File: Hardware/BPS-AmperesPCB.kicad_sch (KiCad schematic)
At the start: 54 parts, among them IC1 INA241A5IDR, IC5 AMC1350DWVR, J1 Discharge V_In, J2 PeripheralCAN, J3 Charge V_In, J4 PeripheralCAN, J5 Shunt Conn, U1 INA145UA/2K5, U2 AMC1300BDWV, U6 TLV6001DCK

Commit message: comments
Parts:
- removed LOGO1: aniMegamind, UTSVT_Logos:Hallock_Image_Small, symbol utsvt-misc:Logo_Placeholder
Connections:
- net OUTN: no longer names the net of R5.2
- net OUTP: no longer names the net of R7.2
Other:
- note added: "Gain: 2.5 V/V (??) Vout = 2.5(VoutP - VoutN) + Vref Cutoff freq: figure out Output voltage range: 0 - 3.3V"
- note added: "TODO: use full 5V input ?? - buck and ldo to 5V"
- note added: "integrate jumper later"
- note removed: "Gain: 2.5 V/V (??) Vout = 2.5(VoutP - VoutN) + Vref Cutoff freq: figure out"
- note removed: "TODO: use full 5V input - buck and ldo to 5V"
- moved on the sheet: H1, H2
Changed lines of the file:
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@@
 	(text "Gain: 0.4 V/V\nInput Voltage Range: 0 - 3.3 V\nOutput Voltage Range: 0 - 1.32 V"
 		(exclude_from_sim no)
-		(at 139.7 130.81 0)
+		(at 139.7 134.62 0)
 		(effects
 			(font
@@
 	(text "Difference amp\nVout = (R2/R1) * (Vp - Vn)"
 		(exclude_from_sim no)
-		(at 220.98 145.034 0)
+		(at 292.354 138.43 0)
 		(effects
 			(font
@@
 		)
 	)
-	(text "Gain: 2.5 V/V (??)\nVout = 2.5(VoutP - VoutN) + Vref\nCutoff freq: figure out "
+	(text "Gain: 2.5 V/V (??)\nVout = 2.5(VoutP - VoutN) + Vref\nCutoff freq: figure out \nOutput voltage range: 0 - 3.3V"
 		(exclude_from_sim no)
-		(at 220.98 135.89 0)
+		(at 221.234 134.874 0)
 		(effects
 			(font
@@
 		)
 	)
-	(text "TODO: use full 5V input\n- buck and ldo to 5V"
+	(text "TODO: use full 5V input ??\n- buck and ldo to 5V"
 		(exclude_from_sim no)
 		(at 151.13 150.876 0)
@@
 		)
 	)
+	(text "integrate jumper later"
+		(exclude_from_sim no)
+		(at 231.14 53.34 0)
+		(effects
+			(font
+				(size 1.27 1.27)
+			)
+		)
+	)
 	(text "(TBD) Shunt Resistor Between 1 and 2\n- old value was 250 uOhm\n"
 		(exclude_from_sim no)
@@
 		)
 	)
-	(label "OUTN"
-		(at 320.04 99.06 0)
-		(effects
-			(font
-				(size 1.27 1.27)
-			)
-			(justify left bottom)
-		)
-	)
 	(label "CAN_HIGH"
 		(at 170.18 55.88 180)
@@
 		)
 	)
-	(label "OUTP"
-		(at 320.04 106.68 0)
-		(effects
-			(font
-				(size 1.27 1.27)
-			)
-			(justify left bottom)
-		)
-	)
 	(label "V-"
 		(at 222.25 59.69 0)
@@
 	(symbol
 		(lib_id "Mechanical:MountingHole")
-		(at 252.73 48.26 0)
+		(at 252.73 39.37 0)
 		(unit 1)
 		(exclude_from_sim no)
@@
 		(fields_autoplaced yes)
 		(property "Reference" "H2"
-			(at 255.27 46.9899 0)
+			(at 255.27 38.0999 0)
 			(effects
 				(font
@@
 		)
 		(property "Value" "ShuntHole2"
-			(at 255.27 49.5299 0)
+			(at 255.27 40.6399 0)
 			(effects
 				(font
@@
 		)
 		(property "Footprint" ""
-			(at 252.73 48.26 0)
+			(at 252.73 39.37 0)
 			(effects
 				(font
@@
 		)
 		(property "Datasheet" "~"
-			(at 252.73 48.26 0)
+			(at 252.73 39.37 0)
 			(effects
 				(font
@@
 		)
 		(property "Description" "Mounting Hole without connection"
-			(at 252.73 48.26 0)
+			(at 252.73 39.37 0)
 			(effects
 				(font
@@
 	(symbol
 		(lib_id "Mechanical:MountingHole")
-		(at 252.73 40.64 0)
+		(at 252.73 31.75 0)
 		(unit 1)
 		(exclude_from_sim no)
@@
 		(dnp no)
 		(property "Reference" "H1"
-			(at 255.27 39.3699 0)
+			(at 255.27 30.4799 0)
 			(effects
 				(font
@@
 		)
 		(property "Value" "ShuntHole1"
-			(at 255.27 41.9099 0)
+			(at 255.27 33.0199 0)
 			(effects
 				(font
@@
 		)
 		(property "Footprint" ""
-			(at 252.73 40.64 0)
+			(at 252.73 31.75 0)
 			(effects
 				(font
@@
 		)
 		(property "Datasheet" "~"
-			(at 252.73 40.64 0)
+			(at 252.73 31.75 0)
 			(effects
 				(font
@@
 		)
 		(property "Description" "Mounting Hole without connection"
-			(at 252.73 40.64 0)
+			(at 252.73 31.75 0)
 			(effects
 				(font
@@
 	)
 	(symbol
-		(lib_id "utsvt-misc:Logo_Placeholder")
-		(at 252.73 21.59 0)
-		(unit 1)
-		(exclude_from_sim no)
-		(in_bom yes)
-		(on_board yes)
-		(dnp no)
-		(fields_autoplaced yes)
-		(property "Reference" "LOGO1"
-			(at 252.73 17.78 0)
-			(effects
-				(font
-					(size 1.27 1.27)
-				)
-				(hide yes)
-			)
-		)
-		(property "Value" "aniMegamind"
-			(at 256.54 21.5899 0)
-			(effects
-				(font
-					(size 1.27 1.27)
-				)
-				(justify left)
-			)
-		)
-		(property "Footprint" "UTSVT_Logos:Hallock_Image_Small"
-			(at 252.73 19.685 0)
-			(effects
-				(font
-					(size 1.27 1.27)
-				)
-				(hide yes)
-			)
-		)
-		(property "Datasheet" ""
-			(at 252.73 19.685 0)
-			(effects
-				(font
-					(size 1.27 1.27)
-				)
-				(hide yes)
-			)
-		)
-		(property "Description" "Graph footprint placeholder"
-			(at 252.73 21.59 0)
-			(effects
-				(font
-					(size 1.27 1.27)
-				)
-				(hide yes)
-			)
-		)
-		(property "PN" ""
-			(at 252.73 21.59 0)
-			(effects
-				(font
-					(size 1.27 1.27)
-				)
-				(hide yes)
-			)
-		)
-		(property "p/n" ""
-			(at 252.73 21.59 0)
-			(effects
-				(font
-					(size 1.27 1.27)
-				)
-				(hide yes)
-			)
-		)
-		(instances
-			(project "BPS-AmperesPCB"
-				(path "/a452d214-ea00-440d-a445-5d6103fda43a"
-					(reference "LOGO1")
-					(unit 1)
-				)
-			)
-		)
-	)
-	(symbol
 		(lib_id "Device:C")
 		(at 335.28 102.87 0)
@@
 	(symbol
 		(lib_id "utsvt-misc:Logo_Placeholder")
-		(at 252.73 30.48 0)
+		(at 252.73 21.59 0)
 		(unit 1)
 		(exclude_from_sim no)
@@
 		(fields_autoplaced yes)
 		(property "Reference" "LOGO2"
-			(at 252.73 26.67 0)
+			(at 252.73 17.78 0)
 			(effects
 				(font
@@
 		)
 		(property "Value" "solarlogo"
-			(at 256.54 30.4799 0)
+			(at 256.54 21.5899 0)
 			(effects
 				(font
@@
 		)
 		(property "Footprint" "UTSVT_Logos:Hallock_Image_Small"
-			(at 252.73 28.575 0)
+			(at 252.73 19.685 0)
 			(effects
 				(font
@@
 		)
 		(property "Datasheet" ""
-			(at 252.73 28.575 0)
+			(at 252.73 19.685 0)
 			(effects
 				(font
@@
 		)
 		(property "Description" "Graph footprint placeholder"
-			(at 252.73 30.48 0)
+			(at 252.73 21.59 0)
 			(effects
 				(font
@@
 		)
 		(property "PN" ""
-			(at 252.73 30.48 0)
+			(at 252.73 21.59 0)
 			(effects
 				(font
@@
 		)
 		(property "p/n" ""
-			(at 252.73 30.48 0)
+			(at 252.73 21.59 0)
 			(effects
 				(font

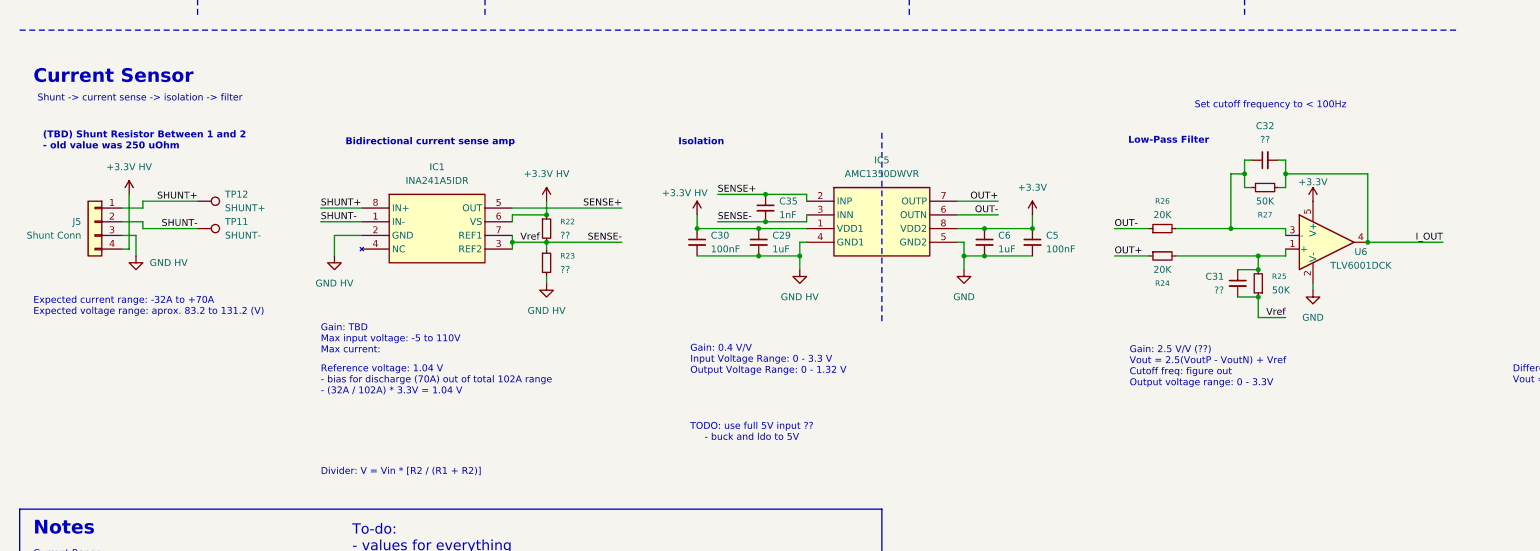
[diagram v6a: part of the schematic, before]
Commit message: changed input into AMC1350, added unity gain buffer
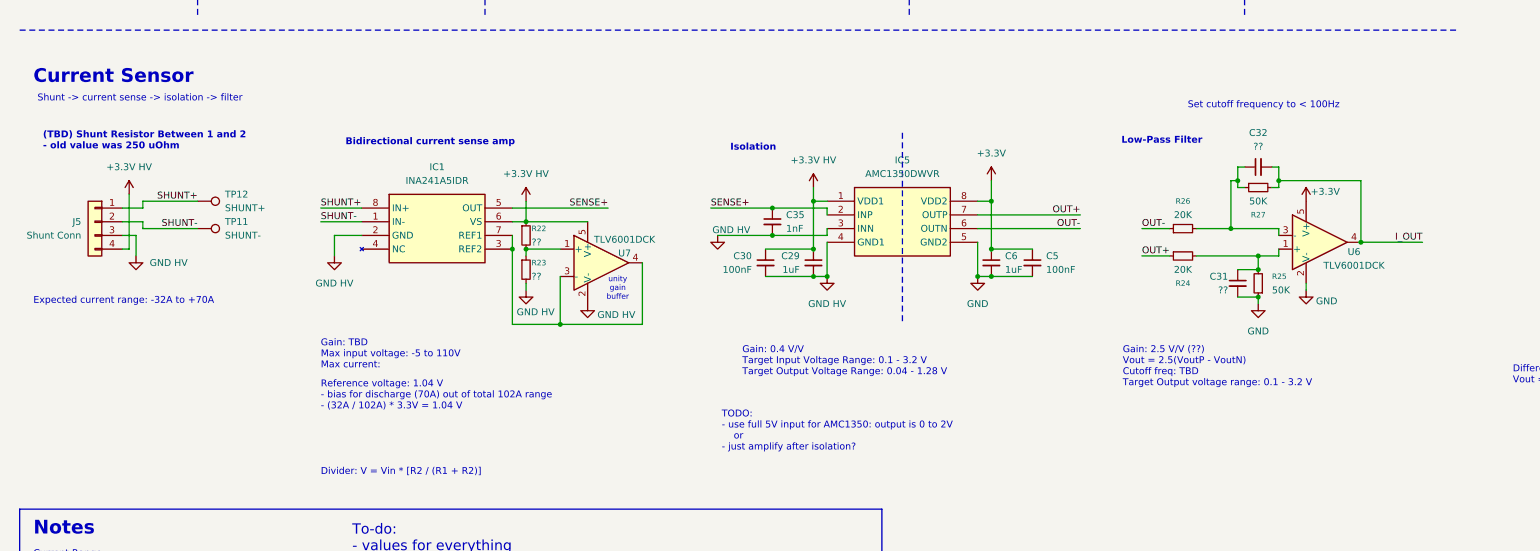
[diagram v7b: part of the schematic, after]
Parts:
- added U7: TLV6001DCK, Package_TO_SOT_SMD:SOT-353_SC-70-5, symbol Amplifier_Operational:TLV6001DCK
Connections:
- net +3.3V HV: now also U7.5 (V+)
- net GND: now also C31.2, R25.1
- net GND HV: now also C35.2, IC5.3 (INN), U7.2 (V-)
- removed net SENSE-: C31.2, C35.2, IC1.3 (REF2), IC1.7 (REF1), IC5.3 (INN), R22.2, R23.1, R25.1
- new net: IC1.3 (REF2), IC1.7 (REF1), U7.3 (-), U7.4
- new net: R22.2, R23.1, U7.1 (+)
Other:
- note added: "Expected current range: -32A to +70A"
- note added: "Gain: 0.4 V/V Target Input Voltage Range: 0.1 - 3.2 V Target Output Voltage Range: 0.04 - 1.28 V"
- note added: "Gain: 2.5 V/V (??) Vout = 2.5(VoutP - VoutN) Cutoff freq: TBD Target Output voltage range: 0.1 - 3.2 V"
- note added: "TODO: - use full 5V input for AMC1350: output is 0 to 2V or - just amplify after isolation?"
- note added: "unity gain buffer"
- note removed: "Expected current range: -32A to +70A Expected voltage range: aprox. 83.2 to 131.2 (V)"
- note removed: "Gain: 0.4 V/V Input Voltage Range: 0 - 3.3 V Output Voltage Range: 0 - 1.32 V"
- note removed: "Gain: 2.5 V/V (??) Vout = 2.5(VoutP - VoutN) + Vref Cutoff freq: figure out Output voltage range: 0 - 3.3V"
- note removed: "TODO: use full 5V input ?? - buck and ldo to 5V"
- moved on the sheet: C29, C30, C32, C35, C5, C6, R22, R23, R24, R26, R27, U6

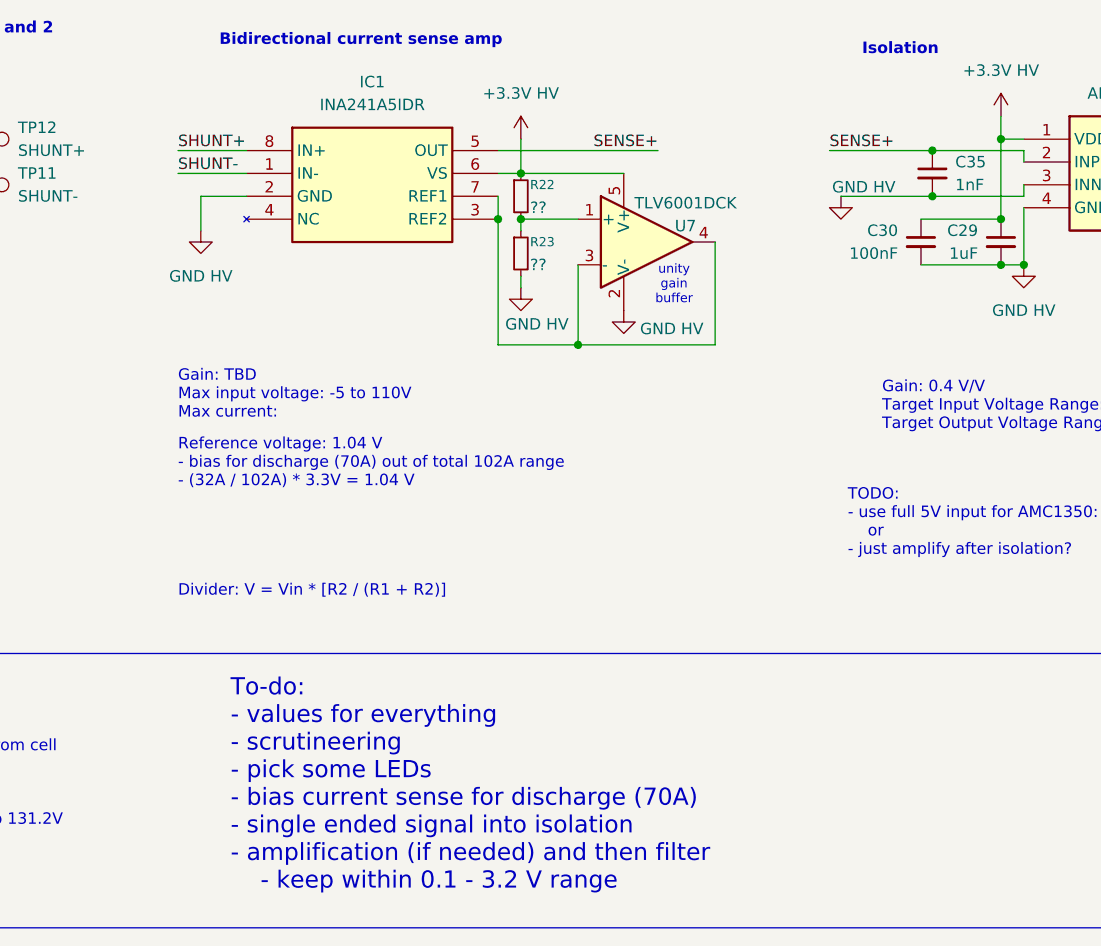
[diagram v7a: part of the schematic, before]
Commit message: added LEDs, changed LDO, still need to address other comments
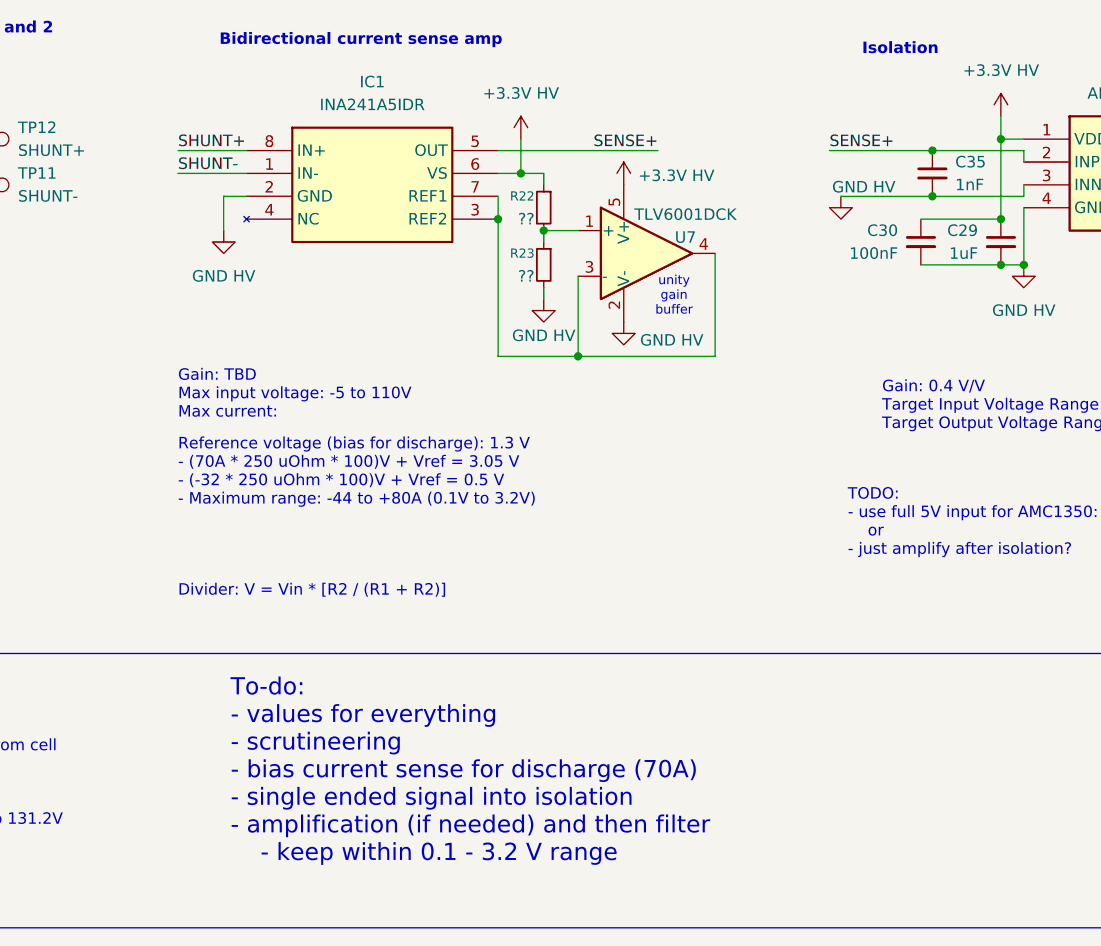
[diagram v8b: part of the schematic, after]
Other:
- note added: "Reference voltage (bias for discharge): 1.3 V - (70A * 250 uOhm * 100)V + Vref = 3.05 V - (-32 * 250 uOhm * 100)V + Vref = 0.5 V - Maximum range: -44 to +80A (0.1V to 3.2V)"
- note added: "To-do: - values for everything - scrutineering - bias current sense for discharge (70A) - single ended signal into isolation - amplification (if needed) and then filter - keep within 0.1 - 3.2 V range"
- note removed: "Reference voltage: 1.04 V - bias for discharge (70A) out of total 102A range - (32A / 102A) * 3.3V = 1.04 V"
- note removed: "To-do: - values for everything - scrutineering - pick some LEDs - bias current sense for discharge (70A) - single ended signal into isolation - amplification (if needed) and then filter - keep within 0.1 - 3.2 V range"
- moved on the sheet: R22, R23, U7
